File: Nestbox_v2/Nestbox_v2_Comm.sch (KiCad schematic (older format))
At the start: 5 parts, among them U501 ESP-12S, U502 RN2483

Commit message: added power footprints, final connector footprints
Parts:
- R501, R502: footprint (none) -> Resistors_SMD:R_0603
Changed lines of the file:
@@
 	9150 4400 9600 4400
 $Comp
-L GND #PWR044
+L GND #PWR045
 U 1 1 59F64207
 P 9150 4850
-F 0 "#PWR044" H 9150 4600 50  0001 C CNN
+F 0 "#PWR045" H 9150 4600 50  0001 C CNN
 F 1 "GND" H 9150 4700 50  0000 C CNN
 F 2 "" H 9150 4850 50  0000 C CNN
@@
 $EndComp
 $Comp
-L GND #PWR045
+L GND #PWR046
 U 1 1 59F64208
 P 7450 4850
-F 0 "#PWR045" H 7450 4600 50  0001 C CNN
+F 0 "#PWR046" H 7450 4600 50  0001 C CNN
 F 1 "GND" H 7450 4700 50  0000 C CNN
 F 2 "" H 7450 4850 50  0000 C CNN
@@
 $EndComp
 $Comp
-L GND #PWR046
+L GND #PWR047
 U 1 1 59F64209
 P 7450 4550
-F 0 "#PWR046" H 7450 4300 50  0001 C CNN
+F 0 "#PWR047" H 7450 4300 50  0001 C CNN
 F 1 "GND" H 7450 4400 50  0000 C CNN
 F 2 "" H 7450 4550 50  0000 C CNN
@@
 $EndComp
 $Comp
-L GND #PWR047
+L GND #PWR048
 U 1 1 59F6420A
 P 7450 4050
-F 0 "#PWR047" H 7450 3800 50  0001 C CNN
+F 0 "#PWR048" H 7450 3800 50  0001 C CNN
 F 1 "GND" H 7450 3900 50  0000 C CNN
 F 2 "" H 7450 4050 50  0000 C CNN
@@
 $EndComp
 $Comp
-L GND #PWR048
+L GND #PWR049
 U 1 1 59F6420B
 P 7450 3700
-F 0 "#PWR048" H 7450 3450 50  0001 C CNN
+F 0 "#PWR049" H 7450 3450 50  0001 C CNN
 F 1 "GND" H 7450 3550 50  0000 C CNN
 F 2 "" H 7450 3700 50  0000 C CNN
@@
 $EndComp
 $Comp
-L GND #PWR049
+L GND #PWR050
 U 1 1 59F6420C
 P 9150 3700
-F 0 "#PWR049" H 9150 3450 50  0001 C CNN
+F 0 "#PWR050" H 9150 3450 50  0001 C CNN
 F 1 "GND" H 9150 3550 50  0000 C CNN
 F 2 "" H 9150 3700 50  0000 C CNN
@@
 $EndComp
 $Comp
-L GND #PWR050
+L GND #PWR051
 U 1 1 59F6420D
 P 9150 4100
-F 0 "#PWR050" H 9150 3850 50  0001 C CNN
+F 0 "#PWR051" H 9150 3850 50  0001 C CNN
 F 1 "GND" H 9150 3950 50  0000 C CNN
 F 2 "" H 9150 4100 50  0000 C CNN
@@
 $EndComp
 $Comp
-L GND #PWR051
+L GND #PWR052
 U 1 1 59F6420E
 P 9150 4250
-F 0 "#PWR051" H 9150 4000 50  0001 C CNN
+F 0 "#PWR052" H 9150 4000 50  0001 C CNN
 F 1 "GND" H 9150 4100 50  0000 C CNN
 F 2 "" H 9150 4250 50  0000 C CNN
@@
 $EndComp
 $Comp
-L GND #PWR052
+L GND #PWR053
 U 1 1 59F6420F
 P 8600 3150
-F 0 "#PWR052" H 8600 2900 50  0001 C CNN
+F 0 "#PWR053" H 8600 2900 50  0001 C CNN
 F 1 "GND" H 8600 3000 50  0000 C CNN
 F 2 "" H 8600 3150 50  0000 C CNN
@@
 $EndComp
 $Comp
-L GND #PWR053
+L GND #PWR054
 U 1 1 59F64210
 P 8500 3150
-F 0 "#PWR053" H 8500 2900 50  0001 C CNN
+F 0 "#PWR054" H 8500 2900 50  0001 C CNN
 F 1 "GND" H 8500 3000 50  0000 C CNN
 F 2 "" H 8500 3150 50  0000 C CNN
@@
 $EndComp
 $Comp
-L GND #PWR054
+L GND #PWR055
 U 1 1 59F64211
 P 8300 3150
-F 0 "#PWR054" H 8300 2900 50  0001 C CNN
+F 0 "#PWR055" H 8300 2900 50  0001 C CNN
 F 1 "GND" H 8300 3000 50  0000 C CNN
 F 2 "" H 8300 3150 50  0000 C CNN
@@
 $EndComp
 $Comp
-L GND #PWR055
+L GND #PWR056
 U 1 1 59F64212
 P 8100 3150
-F 0 "#PWR055" H 8100 2900 50  0001 C CNN
+F 0 "#PWR056" H 8100 2900 50  0001 C CNN
 F 1 "GND" H 8100 3000 50  0000 C CNN
 F 2 "" H 8100 3150 50  0000 C CNN
@@
 $EndComp
 $Comp
-L GND #PWR056
+L GND #PWR057
 U 1 1 59F64213
 P 8000 3150
-F 0 "#PWR056" H 8000 2900 50  0001 C CNN
+F 0 "#PWR057" H 8000 2900 50  0001 C CNN
 F 1 "GND" H 8000 3000 50  0000 C CNN
 F 2 "" H 8000 3150 50  0000 C CNN
@@
 	8400 2850 8400 3150
 $Comp
-L GND #PWR057
+L GND #PWR058
 U 1 1 59F64216
 P 8300 2250
-F 0 "#PWR057" H 8300 2000 50  0001 C CNN
+F 0 "#PWR058" H 8300 2000 50  0001 C CNN
 F 1 "GND" H 8300 2100 50  0000 C CNN
 F 2 "" H 8300 2250 50  0000 C CNN
@@
 $EndComp
 $Comp
-L GND #PWR058
+L GND #PWR059
 U 1 1 59F64217
 P 8500 2250
-F 0 "#PWR058" H 8500 2000 50  0001 C CNN
+F 0 "#PWR059" H 8500 2000 50  0001 C CNN
 F 1 "GND" H 8500 2100 50  0000 C CNN
 F 2 "" H 8500 2250 50  0000 C CNN
@@
 	9450 3950 9150 3950
 $Comp
-L +3.3V #PWR059
+L +3.3V #PWR060
 U 1 1 59F64218
 P 6900 3400
-F 0 "#PWR059" H 6900 3250 50  0001 C CNN
+F 0 "#PWR060" H 6900 3250 50  0001 C CNN
 F 1 "+3.3V" H 6900 3540 50  0000 C CNN
 F 2 "" H 6900 3400 50  0000 C CNN
@@
 $EndComp
 $Comp
-L +3.3V #PWR060
+L +3.3V #PWR061
 U 1 1 59F64219
 P 7050 4150
-F 0 "#PWR060" H 7050 4000 50  0001 C CNN
+F 0 "#PWR061" H 7050 4000 50  0001 C CNN
 F 1 "+3.3V" H 7050 4290 50  0000 C CNN
 F 2 "" H 7050 4150 50  0000 C CNN
@@
 $EndComp
 $Comp
-L +3.3V #PWR061
+L +3.3V #PWR062
 U 1 1 59F6421A
 P 9450 3950
-F 0 "#PWR061" H 9450 3800 50  0001 C CNN
+F 0 "#PWR062" H 9450 3800 50  0001 C CNN
 F 1 "+3.3V" H 9450 4090 50  0000 C CNN
 F 2 "" H 9450 3950 50  0000 C CNN
@@
 F 0 "R502" H 6970 3596 50  0000 L CNN
 F 1 "10K" H 6970 3505 50  0000 L CNN
-F 2 "" V 6830 3550 50  0000 C CNN
+F 2 "Resistors_SMD:R_0603" V 6830 3550 50  0001 C CNN
 F 3 "" H 6900 3550 50  0000 C CNN
 	1    6900 3550
@@
 F 0 "R501" H 2620 5346 50  0000 L CNN
 F 1 "10K" H 2620 5255 50  0000 L CNN
-F 2 "" V 2480 5300 50  0000 C CNN
+F 2 "Resistors_SMD:R_0603" V 2480 5300 50  0001 C CNN
 F 3 "" H 2550 5300 50  0000 C CNN
 	1    2550 5300
@@
 $EndComp
 $Comp
-L +3.3V #PWR062
+L +3.3V #PWR063
 U 1 1 59FF5EE6
 P 2550 5100
-F 0 "#PWR062" H 2550 4950 50  0001 C CNN
+F 0 "#PWR063" H 2550 4950 50  0001 C CNN
 F 1 "+3.3V" H 2565 5273 50  0000 C CNN
 F 2 "" H 2550 5100 50  0000 C CNN
@@
 	2550 5500 2700 5500
 $Comp
-L +3.3V #PWR063
+L +3.3V #PWR064
 U 1 1 59FF5FCD
 P 2550 6200
-F 0 "#PWR063" H 2550 6050 50  0001 C CNN
+F 0 "#PWR064" H 2550 6050 50  0001 C CNN
 F 1 "+3.3V" V 2565 6328 50  0000 L CNN
 F 2 "" H 2550 6200 50  0000 C CNN
@@
 	2550 6200 2700 6200
 $Comp
-L GND #PWR064
+L GND #PWR065
 U 1 1 59FF60B0
 P 3900 6200
-F 0 "#PWR064" H 3900 5950 50  0001 C CNN
+F 0 "#PWR065" H 3900 5950 50  0001 C CNN
 F 1 "GND" V 3905 6072 50  0000 R CNN
 F 2 "" H 3900 6200 50  0000 C CNN

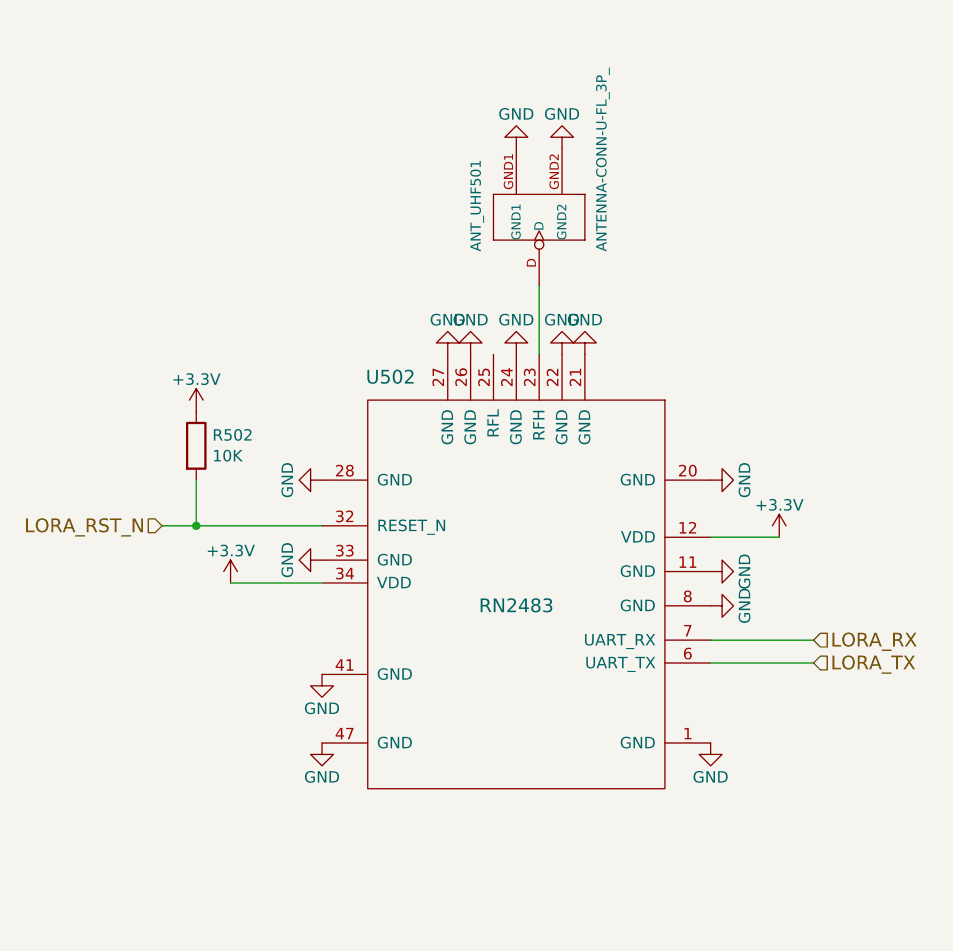
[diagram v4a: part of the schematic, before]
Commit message: all footprints assigned except mosfets; final connectors and their locatino, started component placement
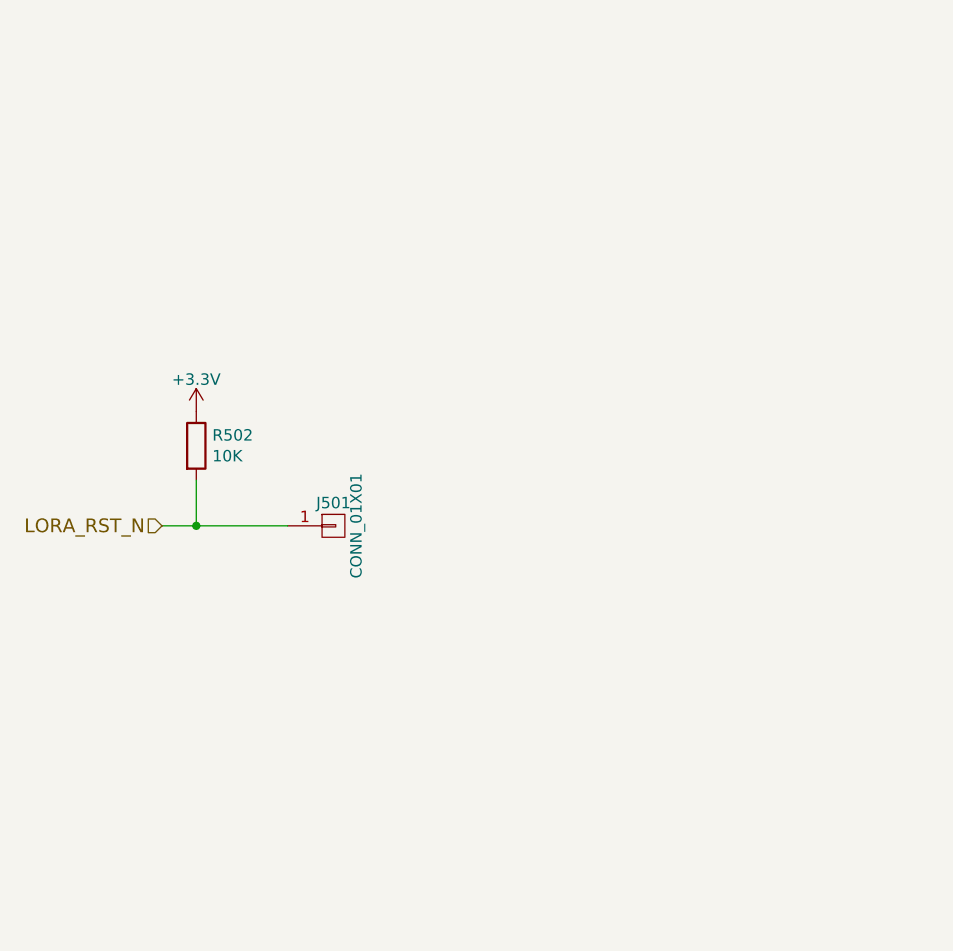
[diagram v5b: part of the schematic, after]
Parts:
- removed ANT_UHF501: ANTENNA-CONN-U-FL_3P_, SeeedOPL-Connector-2016:U-FL3P-SMD-2.6X2.6X1.0MM, symbol ANTENNA-CONN-U-FL_3P_
- removed U502: RN2483, Octanis3:RN2483, symbol RN2483
- added J501: CONN_01X01, Pin_Headers:Pin_Header_Straight_1x01_Pitch2.54mm, symbol CONN_01X01
- U501: footprint (none) -> ESP8266:ESP-12E_SMD
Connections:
- net LORA_RST_N: now also J501.1 (P1)

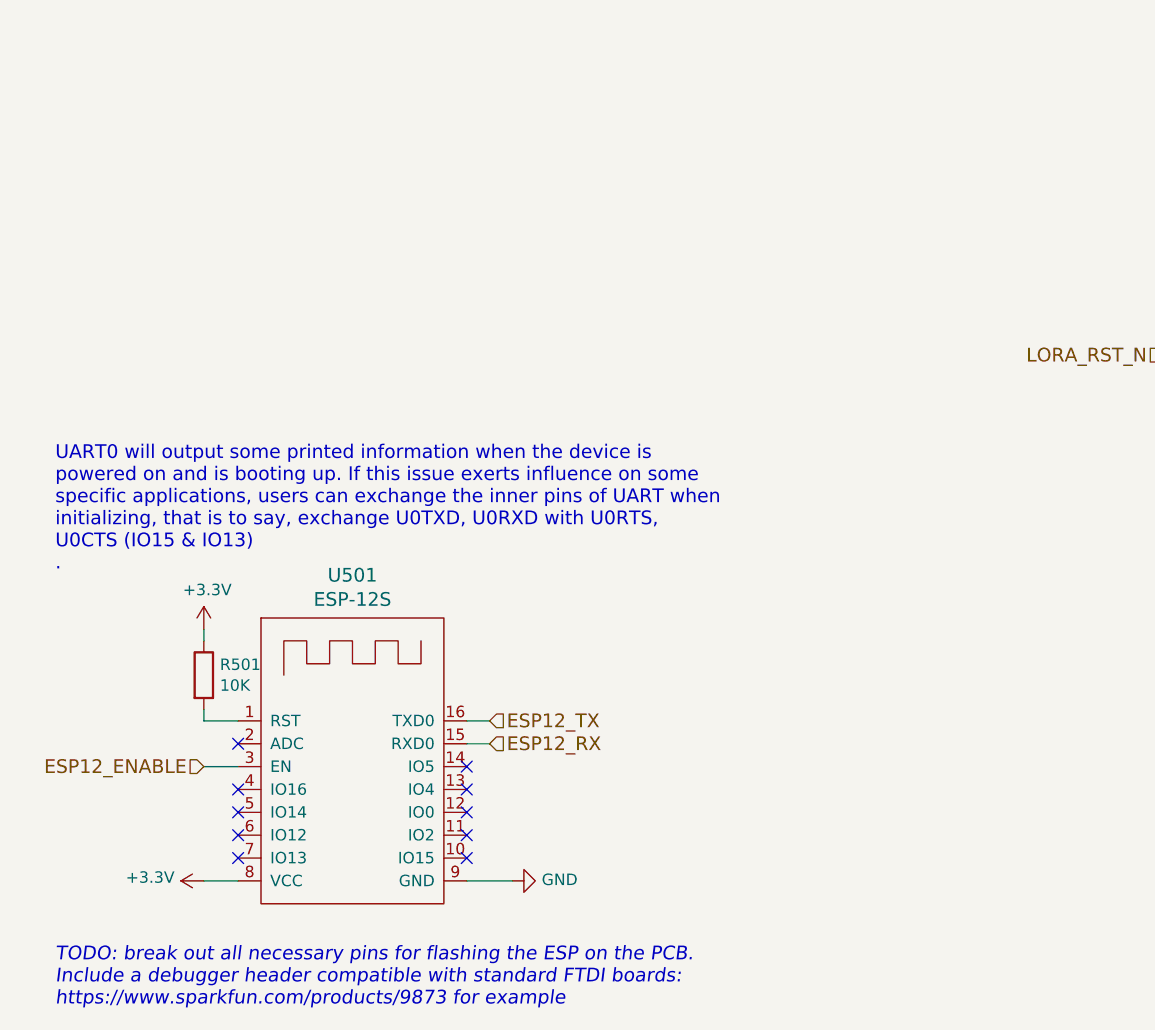
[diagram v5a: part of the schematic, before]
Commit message: ESP footprint to the essential and broke out programming pins
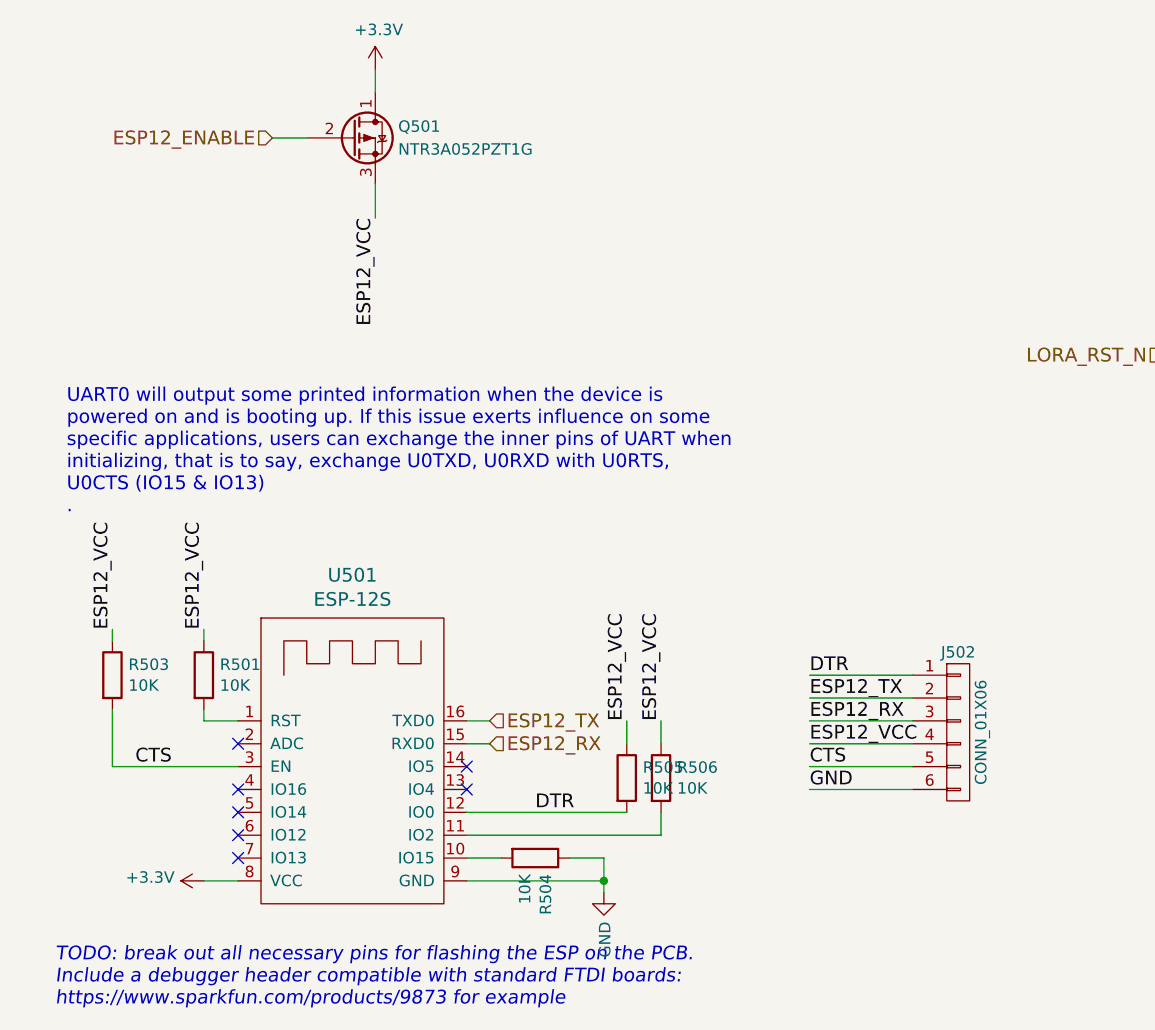
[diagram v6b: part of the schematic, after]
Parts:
- added J502: CONN_01X06, Pin_Headers:Pin_Header_Straight_1x06_Pitch2.54mm, symbol CONN_01X06
- added Q501: NTR3A052PZT1G, TO_SOT_Packages_SMD:SOT-23, symbol Q_PMOS_DGS
- added R503, R504, R505, R506: 10K, Resistors_SMD:R_0603, symbol R
- U501: footprint ESP8266:ESP-12E_SMD -> Octanis3:ESP-12E_SMD_UART_ONLY
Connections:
- net +3V3: now also Q501.1 (D); no longer R501.1
- net ESP12_ENABLE: now also Q501.2 (G); no longer U501.3 (EN)
- net ESP12_RX: now also J502.3 (P3)
- net ESP12_TX: now also J502.2 (P2)
- net GND: now also J502.6 (P6), R504.1
- net at U501.10 (IO15): now also R504.2
- net at U501.11 (IO2): now also R506.2
- net DTR: now reaches U501.12 (IO0)
- net DTR: now also J502.1 (P1), R505.2
- new net CTS: J502.5 (P5), R503.2, U501.3 (EN)
- new net ESP12_VCC: J502.4 (P4), Q501.3 (S), R501.1, R503.1, R505.1, R506.1
- no-connect marks 10 -> 7
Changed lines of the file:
@@
 F 0 "U501" H 3200 5237 60  0000 C CNN
 F 1 "ESP-12S" H 3200 5131 60  0000 C CNN
-F 2 "ESP8266:ESP-12E_SMD" H 2800 5050 60  0001 C CNN
+F 2 "Octanis3:ESP-12E_SMD_UART_ONLY" H 2800 5050 60  0001 C CNN
 F 3 "" H 2800 5050 60  0001 C CNN
 	1    2800 5050
@@
 NoConn ~ 2700 6000
 NoConn ~ 2700 6100
-NoConn ~ 3700 6100
-NoConn ~ 3700 6000
-NoConn ~ 3700 5900
 NoConn ~ 3700 5800
 NoConn ~ 3700 5700
@@
 $Comp
 L +3.3V #PWR046
-U 1 1 59FF5EE6
-P 2550 5100
-F 0 "#PWR046" H 2550 4950 50  0001 C CNN
-F 1 "+3.3V" H 2565 5273 50  0000 C CNN
-F 2 "" H 2550 5100 50  0000 C CNN
-F 3 "" H 2550 5100 50  0000 C CNN
-	1    2550 5100
-	1    0    0    -1
-$EndComp
-Wire Wire Line
-	2550 5100 2550 5150
-Wire Wire Line
-	2550 5450 2550 5500
-Wire Wire Line
-	2550 5500 2700 5500
-$Comp
-L +3.3V #PWR047
 U 1 1 59FF5FCD
 P 2550 6200
-F 0 "#PWR047" H 2550 6050 50  0001 C CNN
+F 0 "#PWR046" H 2550 6050 50  0001 C CNN
 F 1 "+3.3V" V 2565 6328 50  0000 L CNN
 F 2 "" H 2550 6200 50  0000 C CNN
@@
 	0    -1   -1   0
 $EndComp
-Wire Wire Line
-	2550 6200 2700 6200
-$Comp
-L GND #PWR048
+$Comp
+L GND #PWR047
 U 1 1 59FF60B0
-P 3900 6200
-F 0 "#PWR048" H 3900 5950 50  0001 C CNN
-F 1 "GND" V 3905 6072 50  0000 R CNN
-F 2 "" H 3900 6200 50  0000 C CNN
-F 3 "" H 3900 6200 50  0000 C CNN
-	1    3900 6200
-	0    -1   -1   0
-$EndComp
-Wire Wire Line
-	3900 6200 3700 6200
+P 4300 6250
+F 0 "#PWR047" H 4300 6000 50  0001 C CNN
+F 1 "GND" V 4305 6122 50  0000 R CNN
+F 2 "" H 4300 6250 50  0000 C CNN
+F 3 "" H 4300 6250 50  0000 C CNN
+	1    4300 6250
+	1    0    0    -1
+$EndComp
 Text Notes 1900 6850 0    60   Italic 0
 TODO: break out all necessary pins for flashing the ESP on the PCB. \nInclude a debugger header compatible with standard FTDI boards:\nhttps://www.sparkfun.com/products/9873 for example\n\n
-Text Notes 1900 4850 0    60   ~ 0
+Text Notes 1950 4600 0    60   ~ 0
 UART0 will output some printed information when the device is \npowered on and is booting up. If this issue exerts influence on some \nspecific applications, users can exchange the inner pins of UART when \ninitializing, that is to say, exchange U0TXD, U0RXD with U0RTS, \nU0CTS (IO15 & IO13)\n.
 Text HLabel 3800 5500 2    60   Input ~ 0
 ESP12_TX
-Wire Wire Line
-	3800 5500 3700 5500
 Text HLabel 3800 5600 2    60   Input ~ 0
 ESP12_RX
-Wire Wire Line
-	3800 5600 3700 5600
-Text HLabel 2550 5700 0    60   Input ~ 0
+Text HLabel 2850 2950 0    60   Input ~ 0
 ESP12_ENABLE
-Wire Wire Line
-	2550 5700 2700 5700
 Text HLabel 6750 3900 0    60   Input ~ 0
 LORA_RST_N
@@
 $EndComp
 $Comp
-L +3.3V #PWR049
+L +3.3V #PWR048
 U 1 1 59F64218
 P 6900 3400
-F 0 "#PWR049" H 6900 3250 50  0001 C CNN
+F 0 "#PWR048" H 6900 3250 50  0001 C CNN
 F 1 "+3.3V" H 6900 3540 50  0000 C CNN
 F 2 "" H 6900 3400 50  0000 C CNN
@@
 	1    0    0    -1
 $EndComp
-Connection ~ 6900 3900
-Wire Wire Line
-	6900 3900 6900 3700
-Wire Wire Line
-	6750 3900 7300 3900
 $Comp
 L CONN_01X01 J501
@@
 	1    0    0    -1
 $EndComp
+$Comp
+L R R505
+U 1 1 5B158E7F
+P 4400 5750
+F 0 "R505" H 4470 5796 50  0000 L CNN
+F 1 "10K" H 4470 5705 50  0000 L CNN
+F 2 "Resistors_SMD:R_0603" V 4330 5750 50  0001 C CNN
+F 3 "" H 4400 5750 50  0000 C CNN
+	1    4400 5750
+	1    0    0    -1
+$EndComp
+$Comp
+L +3.3V #PWR049
+U 1 1 5B158F7F
+P 3300 2650
+F 0 "#PWR049" H 3300 2500 50  0001 C CNN
+F 1 "+3.3V" H 3315 2823 50  0000 C CNN
+F 2 "" H 3300 2650 50  0000 C CNN
+F 3 "" H 3300 2650 50  0000 C CNN
+	1    3300 2650
+	1    0    0    -1
+$EndComp
+$Comp
+L R R503
+U 1 1 5B1595E2
+P 2150 5300
+F 0 "R503" H 2220 5346 50  0000 L CNN
+F 1 "10K" H 2220 5255 50  0000 L CNN
+F 2 "Resistors_SMD:R_0603" V 2080 5300 50  0001 C CNN
+F 3 "" H 2150 5300 50  0000 C CNN
+	1    2150 5300
+	1    0    0    -1
+$EndComp
+$Comp
+L CONN_01X06 J502
+U 1 1 5B1599BB
+P 5850 5550
+F 0 "J502" H 5850 5900 50  0000 C CNN
+F 1 "CONN_01X06" V 5950 5550 50  0000 C CNN
+F 2 "Pin_Headers:Pin_Header_Straight_1x06_Pitch2.54mm" H 5850 5550 50  0001 C CNN
+F 3 "" H 5850 5550 50  0001 C CNN
+	1    5850 5550
+	1    0    0    -1
+$EndComp
+Text Label 5200 5300 0    60   ~ 0
+DTR
+Text Label 5200 5400 0    60   ~ 0
+ESP12_TX
+Text Label 5200 5500 0    60   ~ 0
+ESP12_RX
+Text Label 5200 5600 0    60   ~ 0
+ESP12_VCC
+Text Label 5200 5700 0    60   ~ 0
+CTS
+Text Label 5200 5800 0    60   ~ 0
+GND
+Text Label 4550 5500 1    60   ~ 0
+ESP12_VCC
+Text Label 4400 5500 1    60   ~ 0
+ESP12_VCC
+Text Label 2550 5100 1    60   ~ 0
+ESP12_VCC
+Text Label 2150 5100 1    60   ~ 0
+ESP12_VCC
+Text Label 2250 5700 0    60   ~ 0
+CTS
+Text Label 4000 5900 0    60   ~ 0
+DTR
+$Comp
+L Q_PMOS_DGS Q501
+U 1 1 5B1510D8
+P 3200 2950
+F 0 "Q501" H 3400 3000 50  0000 L CNN
+F 1 "NTR3A052PZT1G" H 3400 2900 50  0000 L CNN
+F 2 "TO_SOT_Packages_SMD:SOT-23" H 3400 3050 50  0001 C CNN
+F 3 "" H 3200 2950 50  0001 C CNN
+	1    3200 2950
+	1    0    0    -1
+$EndComp
+Text Label 3300 3300 3    60   ~ 0
+ESP12_VCC
+$Comp
+L R R506
+U 1 1 5B158DCF
+P 4550 5750
+F 0 "R506" H 4620 5796 50  0000 L CNN
+F 1 "10K" H 4620 5705 50  0000 L CNN
+F 2 "Resistors_SMD:R_0603" V 4480 5750 50  0001 C CNN
+F 3 "" H 4550 5750 50  0000 C CNN
+	1    4550 5750
+	1    0    0    -1
+$EndComp
+Wire Wire Line
+	2550 5100 2550 5150
+Wire Wire Line
+	2550 5450 2550 5500
+Wire Wire Line
+	2550 5500 2700 5500
+Wire Wire Line
+	2550 6200 2700 6200
+Wire Wire Line
+	3800 5500 3700 5500
+Wire Wire Line
+	3800 5600 3700 5600
+Connection ~ 6900 3900
+Wire Wire Line
+	6900 3900 6900 3700
+Wire Wire Line
+	6750 3900 7300 3900
+Wire Wire Line
+	3700 6000 4550 6000
+Wire Wire Line
+	4550 6000 4550 5900
+Wire Wire Line
+	4550 5500 4550 5600
+Wire Wire Line
+	3700 5900 4400 5900
+Wire Wire Line
+	4400 5500 4400 5600
+Wire Wire Line
+	3700 6100 3850 6100
+Wire Wire Line
+	4300 6100 4300 6250
+Wire Wire Line
+	3700 6200 4300 6200
+Wire Wire Line
+	4150 6100 4300 6100
+Connection ~ 4300 6200
+Wire Wire Line
+	2150 5100 2150 5150
+Wire Wire Line
+	5650 5300 5200 5300
+Wire Wire Line
+	5200 5400 5650 5400
+Wire Wire Line
+	5650 5500 5200 5500
+Wire Wire Line
+	5650 5600 5200 5600
+Wire Wire Line
+	5650 5700 5200 5700
+Wire Wire Line
+	5650 5800 5200 5800
+Wire Wire Line
+	2150 5450 2150 5700
+Wire Wire Line
+	2150 5700 2700 5700
+Wire Wire Line
+	2850 2950 3000 2950
+Wire Wire Line
+	3300 2750 3300 2650
+Wire Wire Line
+	3300 3300 3300 3150
+$Comp
+L R R504
+U 1 1 5B1591D7
+P 4000 6100
+F 0 "R504" H 4070 6146 50  0000 L CNN
+F 1 "10K" H 4070 6055 50  0000 L CNN
+F 2 "Resistors_SMD:R_0603" V 3930 6100 50  0001 C CNN
+F 3 "" H 4000 6100 50  0000 C CNN
+	1    4000 6100
+	0    1    1    0
+$EndComp
 $EndSCHEMATC
